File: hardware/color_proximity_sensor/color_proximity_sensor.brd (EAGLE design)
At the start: 48 x 25 mm, 65 parts, among them IC1 TCS37725FN, IC2 APDS-9800-021, IC4 LM25011MY, IC5 ATXMEGA64DA-AU, J1 PDI_ATMEL_WIDTH, Q1 16 MHz, T1 BC847CDXV6T1G, T4 BC847CDXV6T1G

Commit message: board routed
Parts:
- moved R9 13.0 mm to (14.5, 19.3), turned to 270 degrees
- moved R8 11.9 mm to (16.5, 20.4), turned to 270 degrees
- moved R18 10.0 mm to (38.0, 22.7), turned to 0 degrees
- moved R10 9.51 mm to (17.4, 19.6), flipped to the bottom, turned to 135 degrees
- moved R16 9.48 mm to (36.0, 13.5), turned to 90 degrees
- moved LED3 1.30 mm to (32.5, 3.89)
- moved C3 1.22 mm to (29.7, 2.72)
- moved C33 0.84 mm to (36.5, 3.26)
- moved R60 0.74 mm to (35.3, 6.22), turned to 270 degrees
- moved T4 0.61 mm to (15.6, 5.56)
- moved T1 0.41 mm to (17.3, 1.45), turned to 0 degrees
- moved C15 0.38 mm to (13.0, 14.4)
- moved C12 0.28 mm to (36.5, 19.1), turned to 0 degrees
- moved LED2 0.24 mm to (16.2, 4.37)
- moved LED1 0.23 mm to (20.9, 2.69)
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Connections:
- net +24V: now also COM.7; no longer COM.8
- net APDS_AMBIENT_0-300MV: now also IC5.40; no longer IC5.1
- net APDS_PROXIMITY_ANA_0-0.65V: now also IC5.41; no longer IC5.44
- net BATTERY_MONITOR_0-1V: now also IC5.1; no longer IC5.40
- net COLOR_DATA0_3V3: now also COM.6; no longer COM.3
- net COLOR_DATA1_3V3: now also COM.5; no longer COM.2
- net COLOR_DATA2_3V3: now also COM.4; no longer COM.1
- net COLOR_VALID_OUT_3V3: now also COM.8; no longer COM.4
- net GND: now also COM.1; no longer COM.5
- net LED_GREEN_CMD_3V3: now also IC5.11; no longer IC5.14
- net LED_RED_CMD_3V3: now also IC5.14; no longer IC5.11
- net RX_3V3: now also COM.3; no longer COM.6
- net TX_3V3: now also COM.2; no longer COM.7
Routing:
- net GND: track 92.5 -> 195.9 mm, vias 7 -> 28
- net +24V: track 7.66 -> 98.7 mm, vias 0 -> 7
- net +3V3: track 80.7 -> 153.3 mm, vias 8 -> 13
- net N$11: track 0.00 -> 26.3 mm, vias 0 -> 3
- net N$6: track 0.00 -> 22.4 mm, vias 0 -> 2
- net APDS_PROXIMITY_ANA_0-0.65V: track 7.10 -> 25.0 mm, vias 1 -> 3
- net RX_3V3: track 22.7 -> 34.1 mm
- net APDS_AMBIENT_0-300MV: track 23.6 -> 34.2 mm, vias 1 -> 2
- net N$12: track 0.00 -> 10.6 mm, vias 0 -> 2
- net TX_3V3: track 22.1 -> 30.3 mm
- net BATTERY_MONITOR_0-1V: track 0.00 -> 7.54 mm, vias 0 -> 1
- net COLOR_VALID_OUT_3V3: track 35.3 -> 29.3 mm
- net LED_BLUE_CMD_3V3: track 0.00 -> 5.97 mm, vias 0 -> 1
- net N$5: track 18.6 -> 23.4 mm, vias 1 -> 2
- net COLOR_DATA0_3V3: track 33.4 -> 29.4 mm
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- added copper zone on layer 1, net GND
- added copper zone on layer 16, net GND
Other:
- outline, holes or cut-outs redrawn

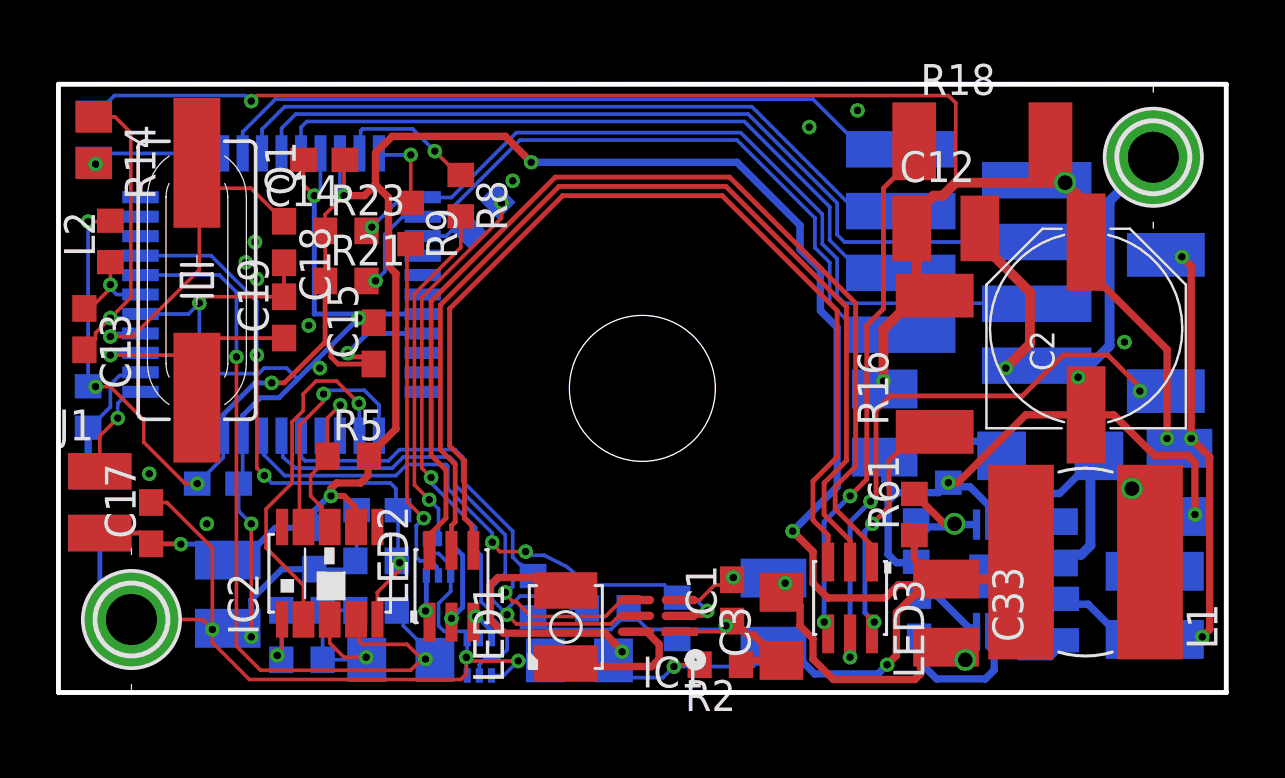
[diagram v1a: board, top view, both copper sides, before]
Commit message: silkscreen done
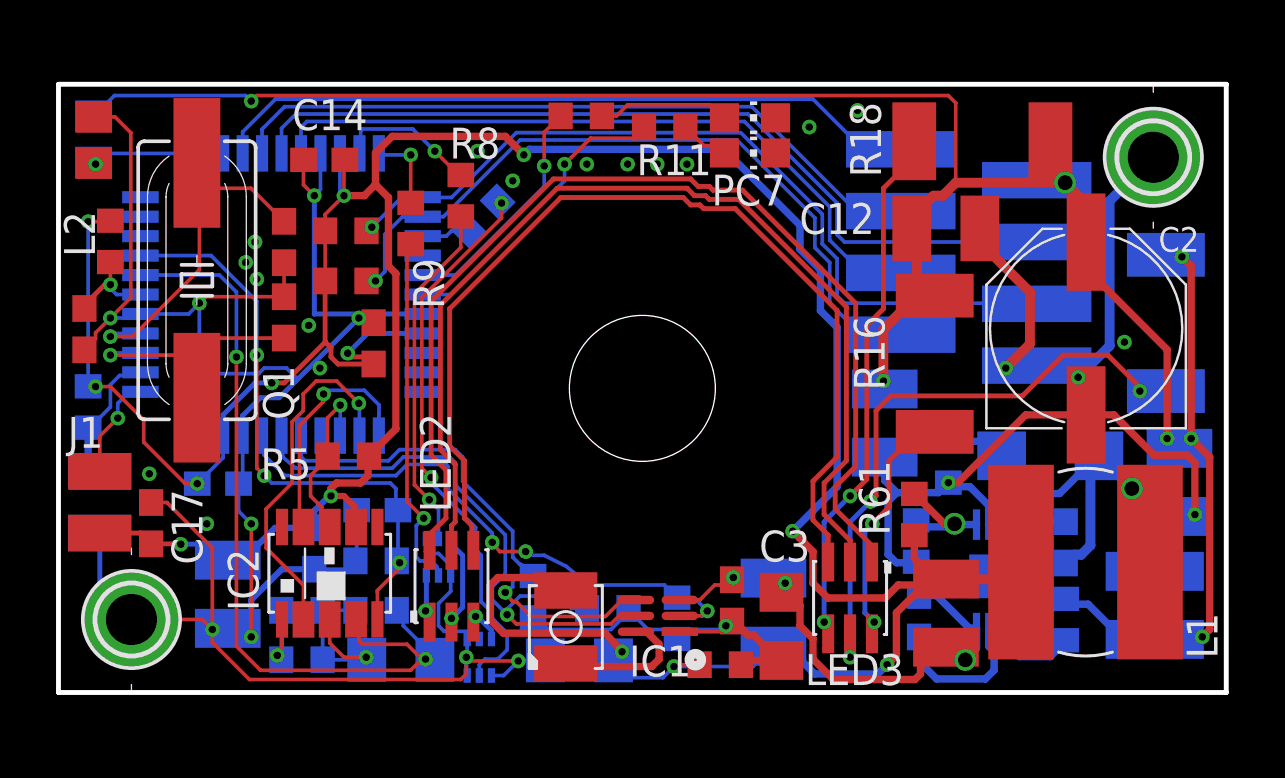
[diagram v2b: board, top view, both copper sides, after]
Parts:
- added PC6, PC7: GREEN, robotter_diode:CHIP-LED0805
- added R11, R12: 270-F, robotter_resistor:R0603
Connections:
- new net N$13: IC5.17, R11.2
- new net N$16: IC5.16, R12.2
- new net N$21: PC7.A, R11.1
- new net N$22: PC6.A, R12.1
- net GND: now also PC6.C, PC7.C
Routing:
- net N$13: track 0.00 -> 12.4 mm, vias 0 -> 1
- net N$16: track 0.00 -> 9.68 mm, vias 0 -> 1
- net N$22: track 0.00 -> 5.42 mm
- net N$21: track 0.00 -> 2.11 mm
- net GND: vias 28 -> 33
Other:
- board text added: "color_prox sens v1"

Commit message: traces modified
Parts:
- moved PC7 1.68 mm to (30.1, 22.2)
- moved R10 0.31 mm to (17.4, 19.9)
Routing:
- net GND: track 195.9 -> 221.2 mm
- net N$21: track 2.11 -> 3.69 mm

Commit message: few changes on board
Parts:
- C33: value 10µF 25V -> 22UF-C_10V
- R20, R25: value 10K-F -> 3K09-F
- moved IC1 1.87 mm to (25.0, 1.32)
- moved R2 1.35 mm to (25.9, 1.52), flipped to the bottom, turned to 0 degrees
- moved IC2 0.76 mm to (10.4, 4.90)
- moved R20 0.72 mm to (25.9, 3.58), turned to 0 degrees
- moved C5 0.70 mm to (29.8, 2.77)
- moved C32 0.46 mm to (41.9, 6.17)
- moved PC7 0.46 mm to (30.6, 22.2)
- moved R58 0.46 mm to (41.9, 3.00)
- moved C1 0.24 mm to (27.8, 3.56)
- moved C15 0.23 mm to (12.7, 14.4)
- moved C3 0.17 mm to (29.8, 2.87)
- moved LED1 0.08 mm to (20.8, 2.69)
- moved LED2 0.08 mm to (16.1, 4.37)
- moved R1 0.08 mm to (19.4, 3.94)
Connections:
- net GND: now also IC4.THERMAL
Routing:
- net GND: track 221.2 -> 225.7 mm, vias 33 -> 40
- net N$4: track 5.76 -> 3.52 mm
- net SCL_3V3: track 24.0 -> 26.1 mm
- net APDS_AMBIENT_0-300MV: track 34.2 -> 35.8 mm
- net N$10: track 44.0 -> 45.0 mm
- net N$14: track 42.4 -> 43.4 mm
- net N$15: track 41.1 -> 42.0 mm
- net SDA_3V3: track 25.6 -> 26.4 mm
- net +3V3: track 153.5 -> 154.2 mm, vias 13 -> 12
- net TCS_VCC: track 16.1 -> 16.7 mm
- net APDS_ENABLE_3V3: track 14.8 -> 15.3 mm

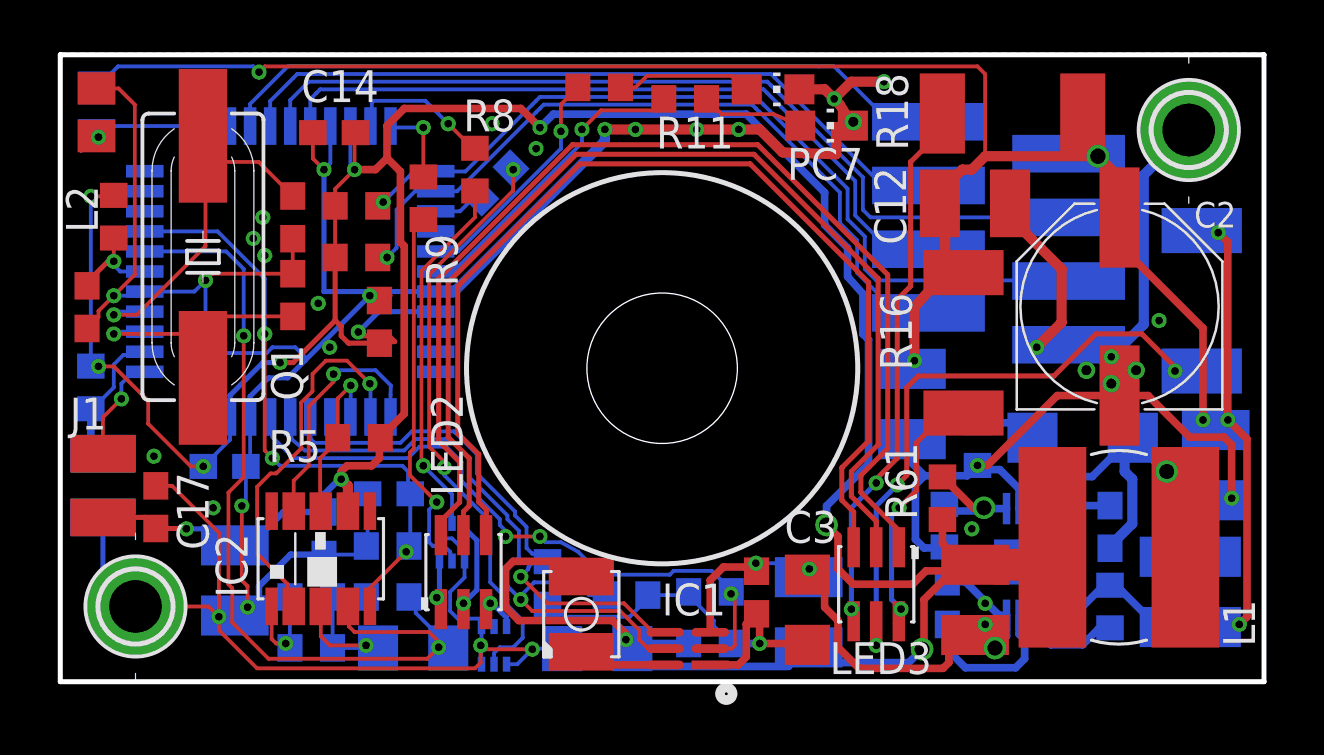
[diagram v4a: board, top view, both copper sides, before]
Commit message: mouser component ref added
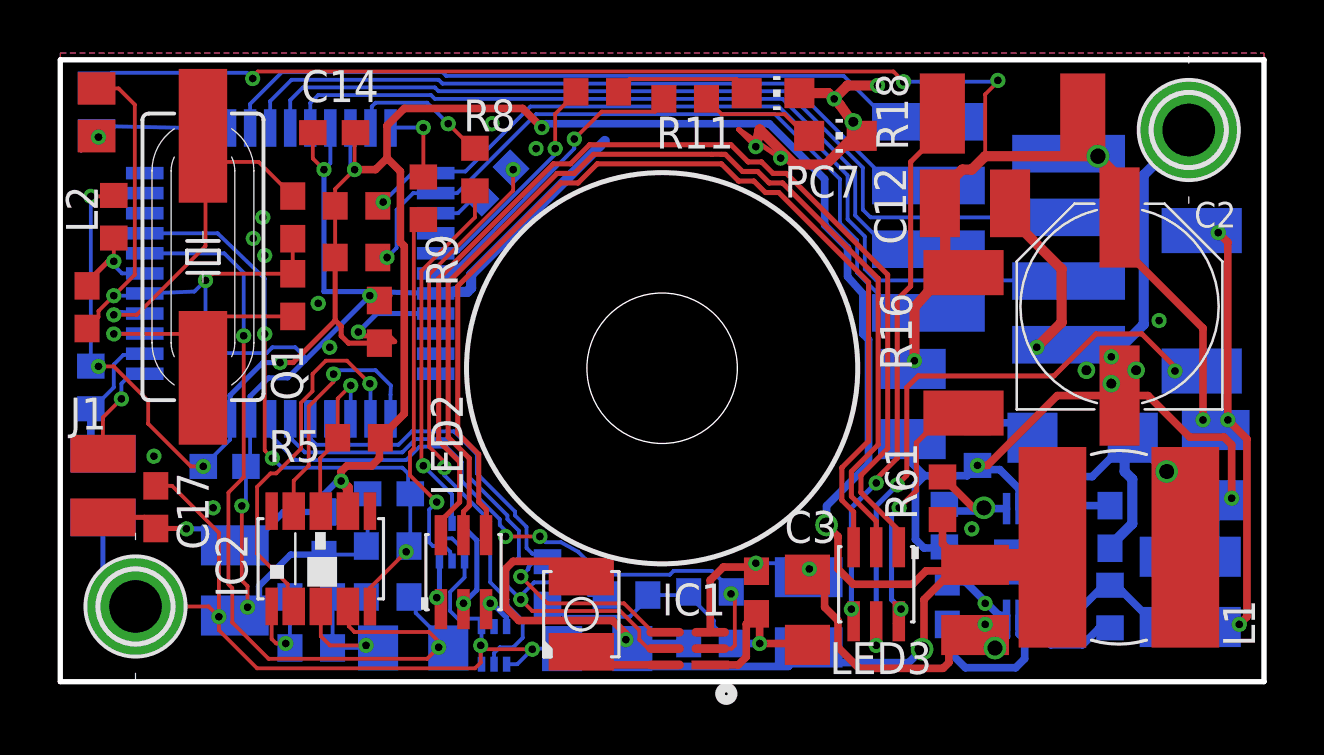
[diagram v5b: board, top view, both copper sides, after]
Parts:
- moved PC7 0.54 mm to (30.9, 21.8)
- moved R12 0.19 mm to (21.4, 23.5)
- moved PC6 0.15 mm to (28.4, 23.5)
- moved IC5 0.08 mm to (9.17, 16.3)
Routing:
- net GND: track 225.7 -> 223.0 mm, vias 40 -> 38
- net N$21: track 4.09 -> 4.70 mm
- net +24V: track 98.9 -> 99.3 mm, vias 7 -> 9
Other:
- board size 48 x 25 mm -> 48 x 24.8 mm
